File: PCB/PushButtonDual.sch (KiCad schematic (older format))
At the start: 3 parts, among them SW2 PCB_Push_Button, SW3 PCB_Push_Button

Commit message: Route more signals
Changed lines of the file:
@@
 $Descr A4 11693 8268
 encoding utf-8
-Sheet 16 23
+Sheet 14 23
 Title "Litter Robot 3 - Push button (dual)"
 Date "2021-04-10"
@@
 AR Path="/603F1F4D/605BE155/604E1842" Ref="R?"  Part="1"
 AR Path="/603F1F4D/605BE15D/604E1842" Ref="R?"  Part="1"
-F 0 "R35" H 5070 3046 50  0000 L CNN
+F 0 "R33" H 5070 3046 50  0000 L CNN
 F 1 "10k" H 5070 2955 50  0000 L CNN
 F 2 "Resistor_SMD:R_0603_1608Metric" V 4930 3000 50  0001 C CNN
@@
 AR Path="/603F1F4D/605BE155/604E185B" Ref="SW?"  Part="1"
 AR Path="/603F1F4D/605BE15D/604E185B" Ref="SW?"  Part="1"
-F 0 "SW6" V 5200 4200 50  0000 L CNN
+F 0 "SW3" V 5200 4200 50  0000 L CNN
 F 1 "PCB_Push_Button" V 5300 4200 50  0000 L CNN
 F 2 "LitterRobot:PCB_Push_Button_5mm_0.4mm" H 5250 4200 50  0001 C CNN
@@
 AR Path="/603F1F4D/605BE155/604E42E5" Ref="SW?"  Part="1"
 AR Path="/603F1F4D/605BE15D/604E42E5" Ref="SW?"  Part="1"
-F 0 "SW5" V 4700 4200 50  0000 L CNN
+F 0 "SW2" V 4700 4200 50  0000 L CNN
 F 1 "PCB_Push_Button" V 4800 4200 50  0000 L CNN
 F 2 "LitterRobot:PCB_Push_Button_5mm_0.4mm" H 4750 4200 50  0001 C CNN

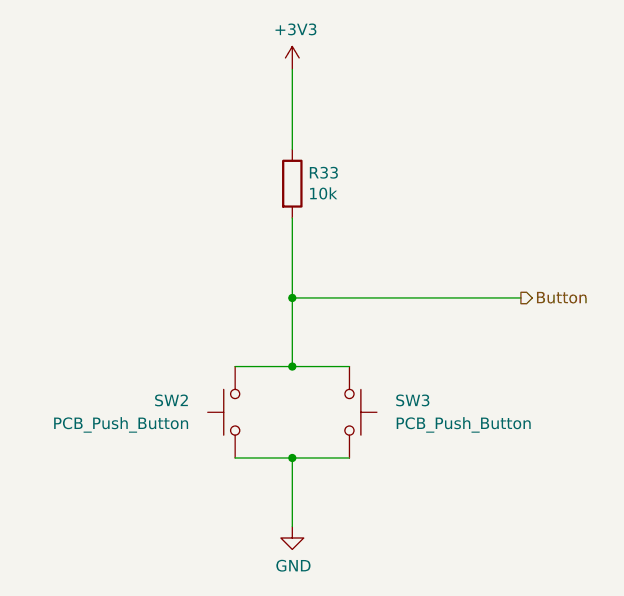
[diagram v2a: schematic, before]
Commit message: Add jumpers on the power supply outputs
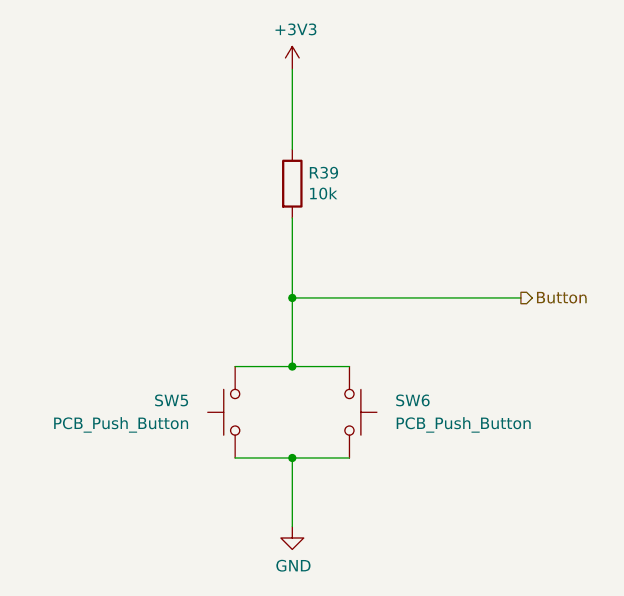
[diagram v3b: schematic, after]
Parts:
- renumbered R33 to R37
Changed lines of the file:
@@
 Sheet 14 23
 Title "Litter Robot 3 - Push button (dual)"
-Date "2021-04-10"
+Date "2021-05-24"
 Rev "A1"
 Comp "L. Sartory"
@@
 AR Path="/603E03AA/603C06CF/604E1842" Ref="R?"  Part="1"
 AR Path="/603E03AA/603C09F0/604E1842" Ref="R?"  Part="1"
-AR Path="/603E03AA/604DE92D/604E1842" Ref="R33"  Part="1"
-AR Path="/603E03AA/604E2A9A/604E1842" Ref="R35"  Part="1"
+AR Path="/603E03AA/604DE92D/604E1842" Ref="R37"  Part="1"
+AR Path="/603E03AA/604E2A9A/604E1842" Ref="R39"  Part="1"
 AR Path="/603F1F4D/605BE155/604E1842" Ref="R?"  Part="1"
 AR Path="/603F1F4D/605BE15D/604E1842" Ref="R?"  Part="1"
-F 0 "R33" H 5070 3046 50  0000 L CNN
+F 0 "R39" H 5070 3046 50  0000 L CNN
 F 1 "10k" H 5070 2955 50  0000 L CNN
 F 2 "Resistor_SMD:R_0603_1608Metric" V 4930 3000 50  0001 C CNN
@@
 AR Path="/603F1F4D/605BE155/604E185B" Ref="SW?"  Part="1"
 AR Path="/603F1F4D/605BE15D/604E185B" Ref="SW?"  Part="1"
-F 0 "SW3" V 5200 4200 50  0000 L CNN
+F 0 "SW6" V 5200 4200 50  0000 L CNN
 F 1 "PCB_Push_Button" V 5300 4200 50  0000 L CNN
 F 2 "LitterRobot:PCB_Push_Button_5mm_0.4mm" H 5250 4200 50  0001 C CNN
@@
 AR Path="/603F1F4D/605BE155/604E42E5" Ref="SW?"  Part="1"
 AR Path="/603F1F4D/605BE15D/604E42E5" Ref="SW?"  Part="1"
-F 0 "SW2" V 4700 4200 50  0000 L CNN
+F 0 "SW5" V 4700 4200 50  0000 L CNN
 F 1 "PCB_Push_Button" V 4800 4200 50  0000 L CNN
 F 2 "LitterRobot:PCB_Push_Button_5mm_0.4mm" H 4750 4200 50  0001 C CNN
